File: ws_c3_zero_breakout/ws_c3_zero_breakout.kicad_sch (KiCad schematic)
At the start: 10 parts, among them J1 LEFT WING, J2 RIGHT WING, U1 QMI8658C, U2 QMC5883L

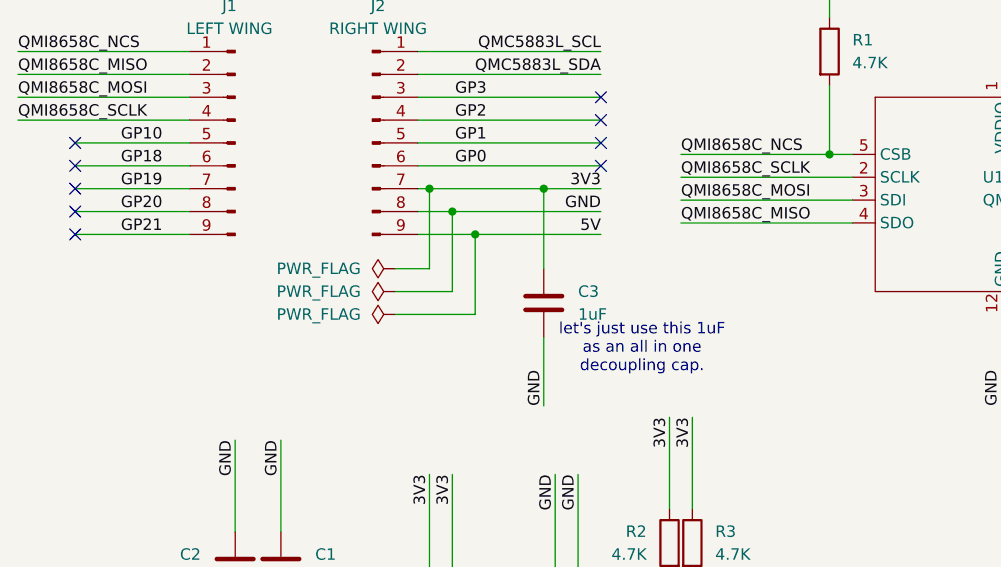
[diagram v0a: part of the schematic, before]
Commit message: comment and label change
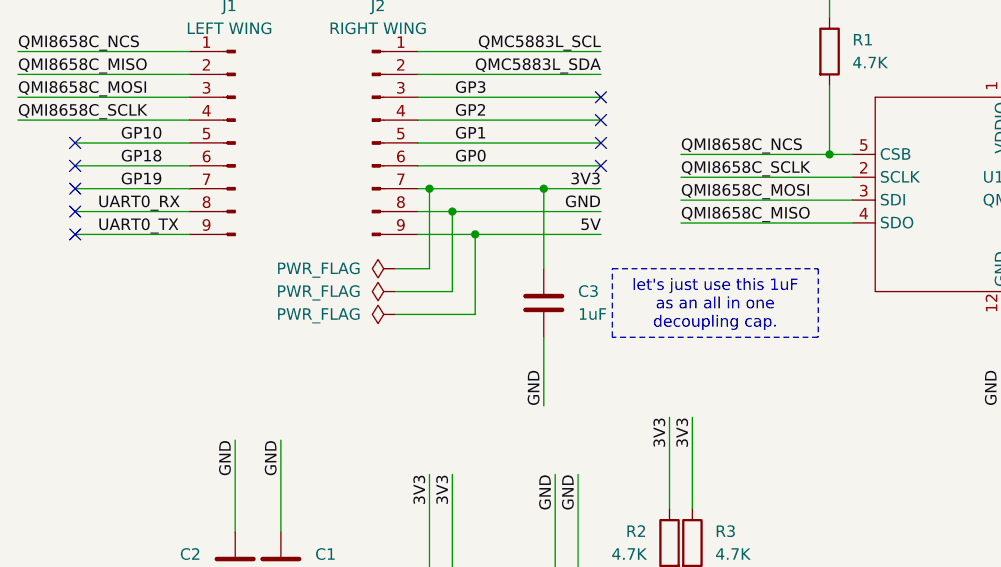
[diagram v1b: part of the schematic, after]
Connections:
- net GP20 renamed UART0_RX
- net GP21 renamed UART0_TX
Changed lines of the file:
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@@
 	(generator_version "10.0")
 	(paper "A4")
+	(rectangle
+		(start 83.82 52.07)
+		(end 106.68 59.69)
+		(stroke
+			(width 0)
+			(type dot)
+		)
+		(fill
+			(type none)
+		)
+	)
 	(text "let's just use this 1uF\nas an all in one\ndecoupling cap."
 		(exclude_from_sim no)
-		(at 87.122 60.96 0)
+		(at 95.25 56.134 0)
 		(effects
 			(font
@@
 		)
 	)
-	(label "GP20"
-		(at 29.21 45.72 0)
+	(label "UART0_RX"
+		(at 26.67 45.72 0)
 		(effects
 			(font
@@
 		)
 	)
-	(label "GP21"
-		(at 29.21 48.26 0)
-		(effects
-			(font
+	(label "UART0_TX"
+		(at 26.67 48.26 0)
+		(effects
+			(font

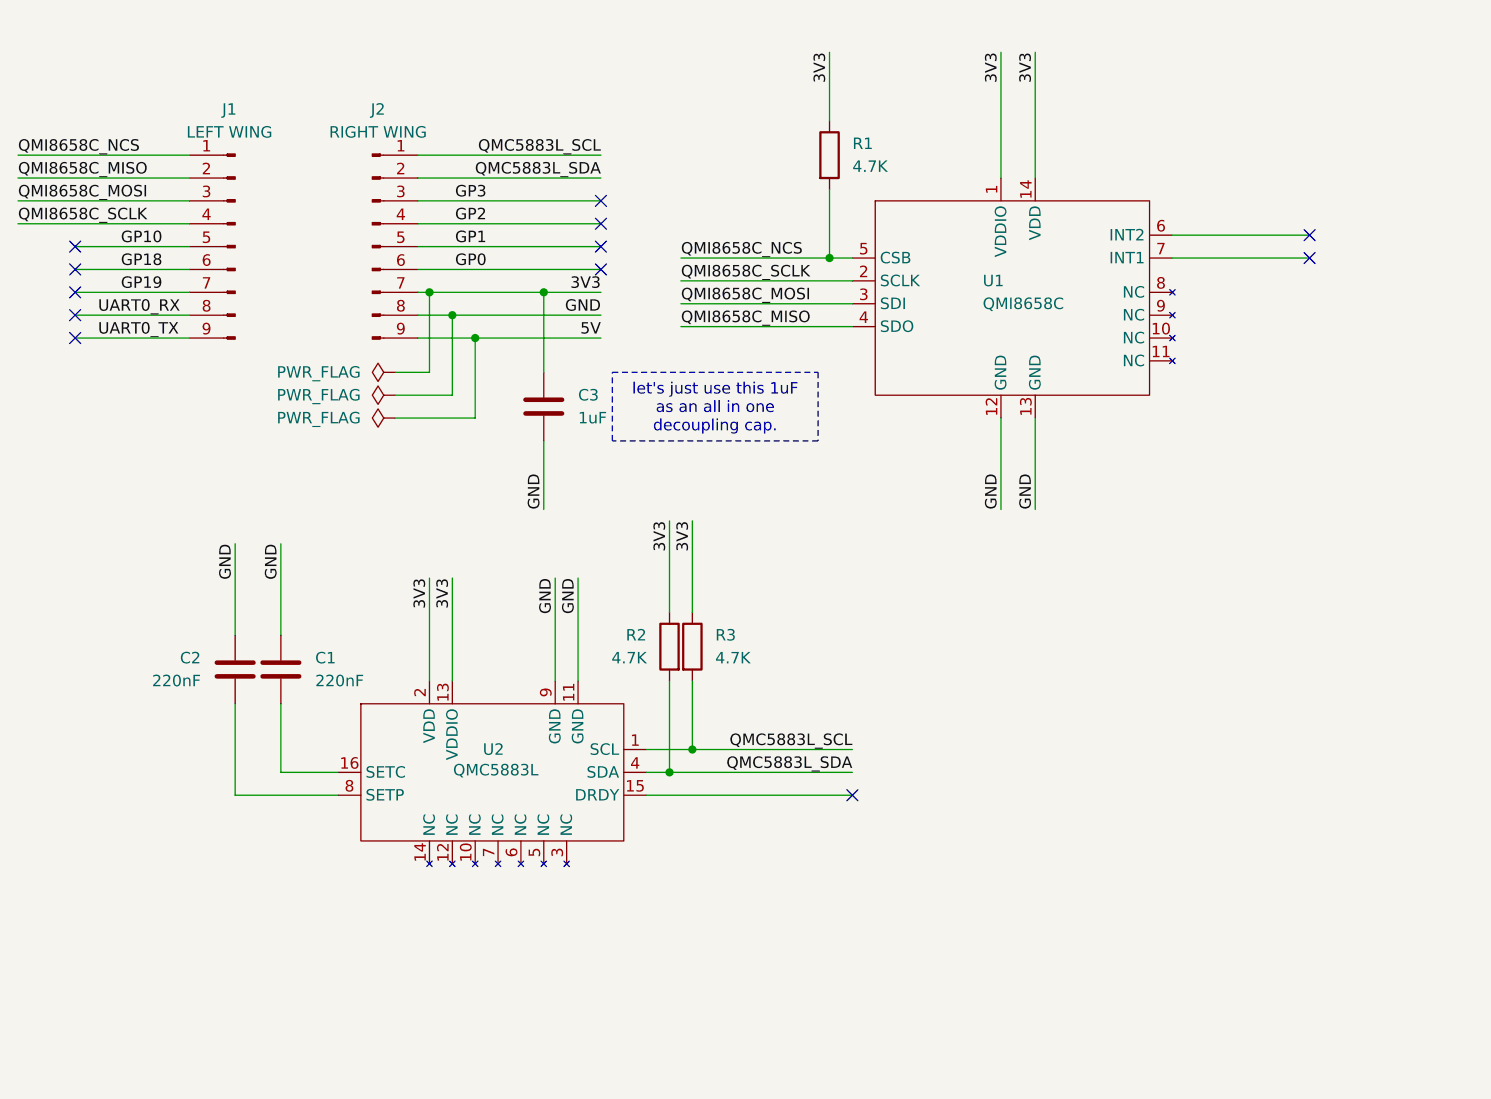
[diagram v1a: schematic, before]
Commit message: fixing major pin map  bug in symbol
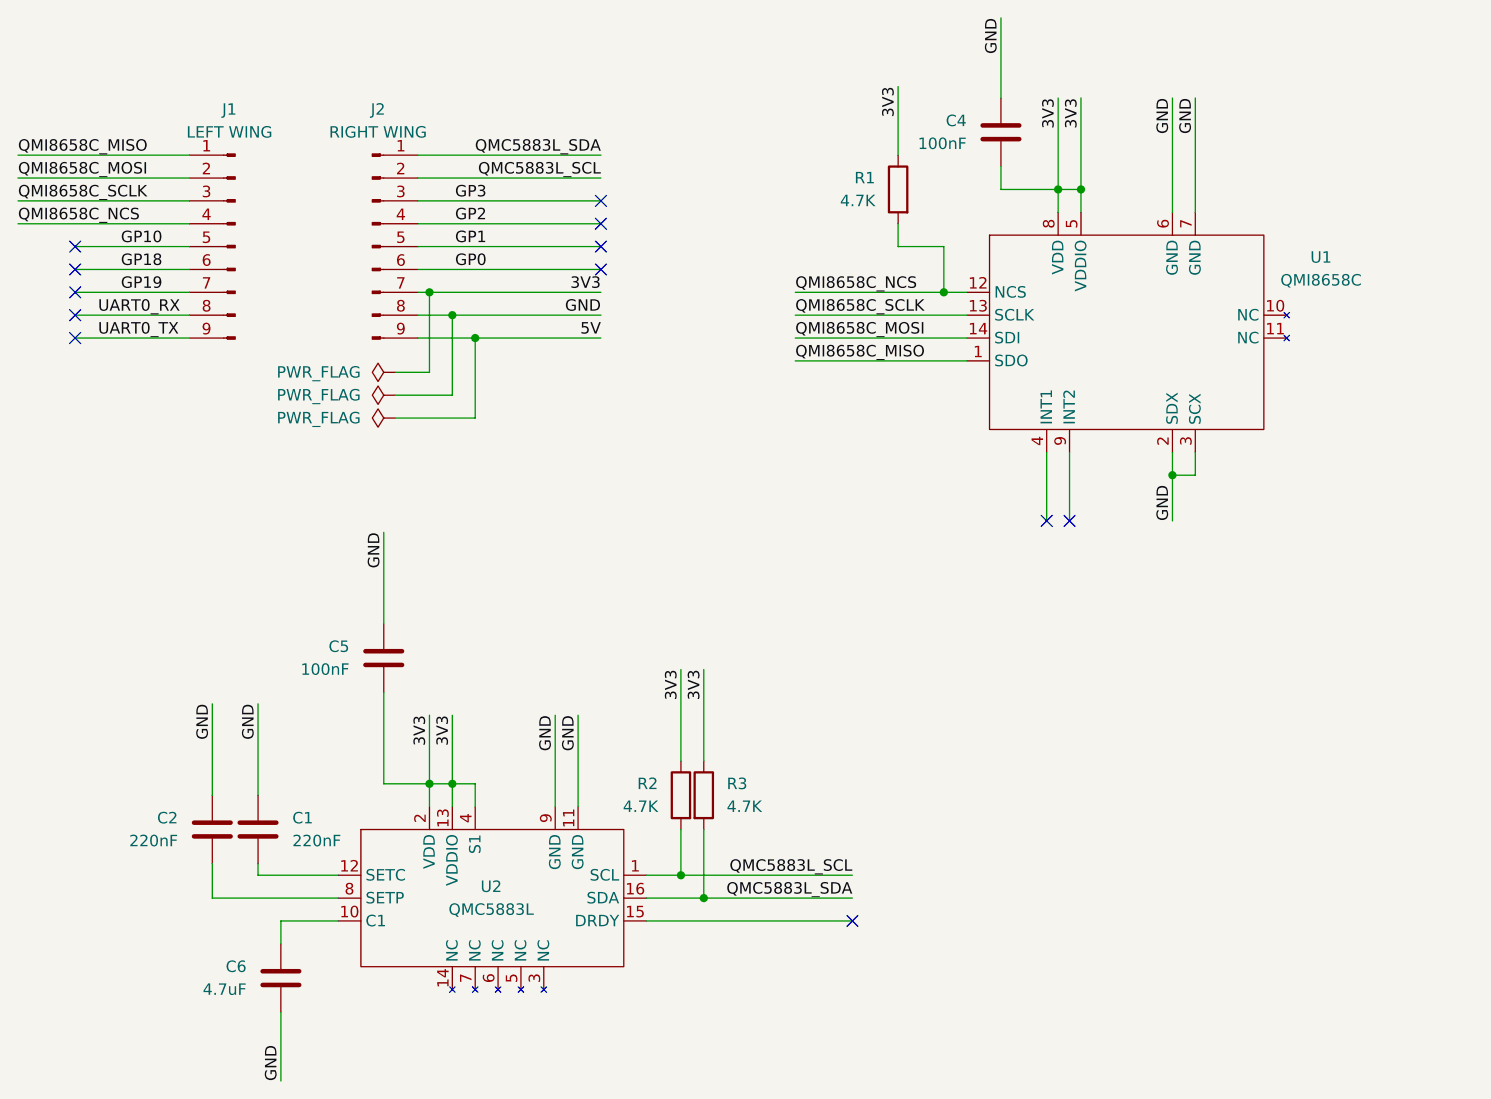
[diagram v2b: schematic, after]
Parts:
- removed C3: 1uF, Capacitor_SMD:C_0603_1608Metric, symbol Device:C
- added C4, C5: 100nF, Capacitor_SMD:C_0603_1608Metric, symbol Device:C
- added C6: 4.7uF, Capacitor_SMD:C_0603_1608Metric, symbol Device:C
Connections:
- net 3V3: now also U1.5 (VDDIO), U1.8 (VDD), U2.4 (S1), C4.2, C5.2; no longer U1.1 (VDDIO), U1.14 (VDD)
- net GND: now also U1.2 (SDX), U1.3 (SCX), U1.6 (GND), U1.7 (GND), C4.1, C5.1, C6.2; no longer U1.12 (GND), U1.13 (GND)
- net QMC5883L_SCL: now also J2.2 (Pin_2), R2.2; no longer J2.1 (Pin_1), R3.2
- net QMC5883L_SDA: now also J2.1 (Pin_1), R3.2, U2.16 (SDA); no longer J2.2 (Pin_2), R2.2, U2.4 (SDA)
- net QMI8658C_MISO: now also J1.1 (Pin_1), U1.1 (SDO); no longer J1.2 (Pin_2), U1.4 (SDO)
- net QMI8658C_MOSI: now also J1.2 (Pin_2), U1.14 (SDI); no longer J1.3 (Pin_3), U1.3 (SDI)
- net QMI8658C_NCS: now also J1.4 (Pin_4), U1.12 (NCS); no longer J1.1 (Pin_1), U1.5 (CSB)
- net QMI8658C_SCLK: now also J1.3 (Pin_3), U1.13 (SCLK); no longer J1.4 (Pin_4), U1.2 (SCLK)
- net at U2.10 (C1): now also C6.1
- net at U2.12 (SETC): now also C1.2
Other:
- note removed: "let's just use this 1uF as an all in one decoupling cap."
- moved on the sheet: C1, C2, R1, R2, R3

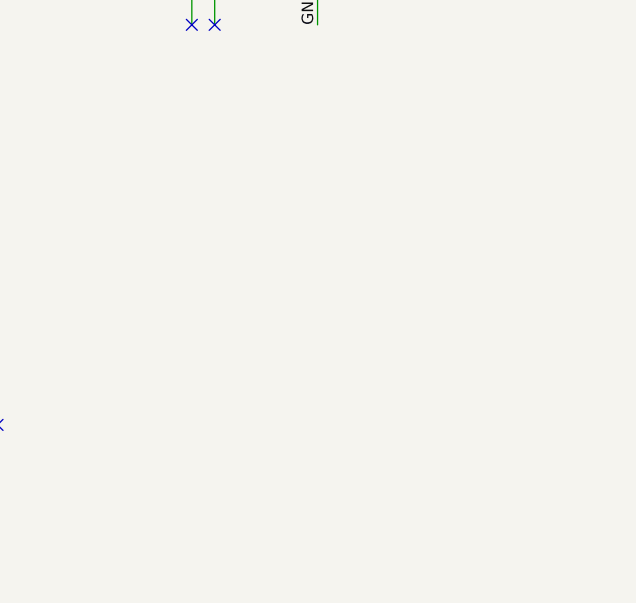
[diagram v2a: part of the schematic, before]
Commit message: adding bmp280
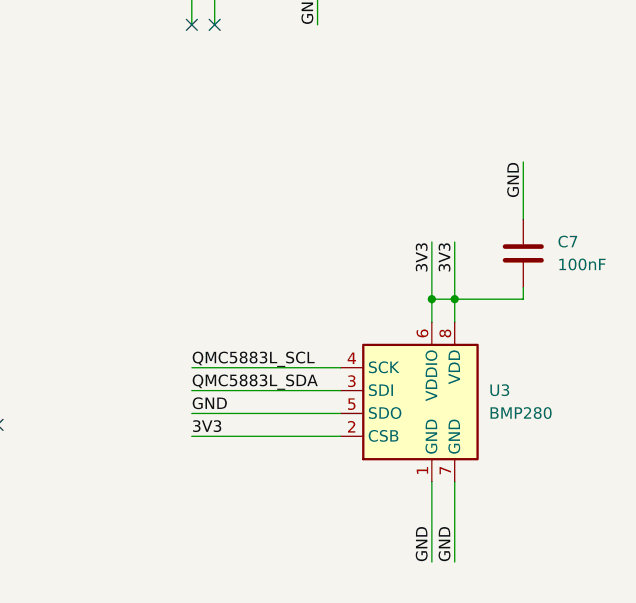
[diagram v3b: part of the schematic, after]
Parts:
- added C7: 100nF, Capacitor_SMD:C_0603_1608Metric, symbol Device:C
- added U3: BMP280, Package_LGA:Bosch_LGA-8_2x2.5mm_P0.65mm_ClockwisePinNumbering, symbol Sensor_Pressure:BMP280
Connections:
- net 3V3: now also C7.2, U3.2 (CSB), U3.6 (VDDIO), U3.8 (VDD)
- net GND: now also C7.1, U3.1 (GND), U3.5 (SDO), U3.7 (GND)
- net QMC5883L_SCL: now also U3.4 (SCK)
- net QMC5883L_SDA: now also U3.3 (SDI)
